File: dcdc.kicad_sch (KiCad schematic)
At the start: 199 parts, among them U11 SIC431AED-T1-GE3, U12 SIC431AED-T1-GE3, U13 SIC431AED-T1-GE3, U22 INA219AIDCNR, U50 INA219AIDCNR, U60 INA219AIDCNR, U65 SIC431AED-T1-GE3, U66 INA219AIDCNR, U69 TPS564247DRLR, U7 TPS564247DRLR, U75 SIC431AED-T1-GE3, U76 INA219AIDCNR, U8 SIC431AED-T1-GE3

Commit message: Update naming on schematic sheets and PCB, update release date
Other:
- title: Jetson AGX Thor Baseboard -> Antmicro Baseboard for Jetson AGX Thor
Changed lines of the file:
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@@
 	(paper "A3")
 	(title_block
-		(title "Jetson AGX Thor Baseboard")
-		(date "2025-11-03")
+		(title "Antmicro Baseboard for Jetson AGX Thor")
+		(date "2026-02-17")
 		(rev "1.1.0")
 		(company "Antmicro Ltd")

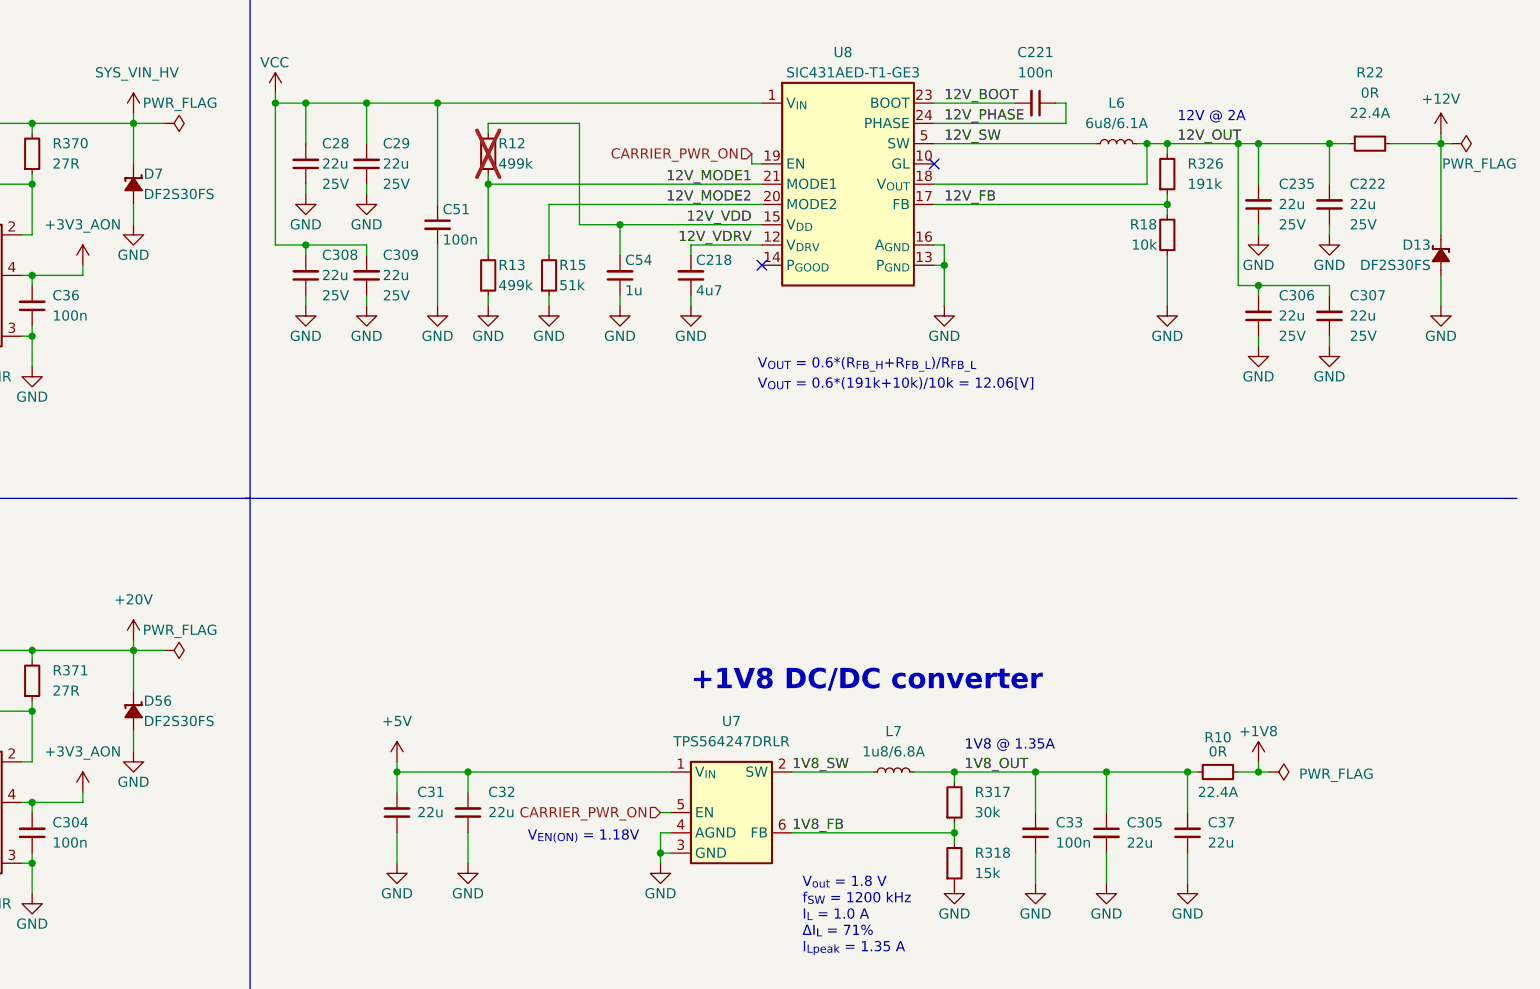
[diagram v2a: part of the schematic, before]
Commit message: [#88664] DF2S30FS diodes replaced by ESDA25P35-1U1M
DF2S30FS -> ESDA25P35-1U1M, changes done on schematics and PCB editor
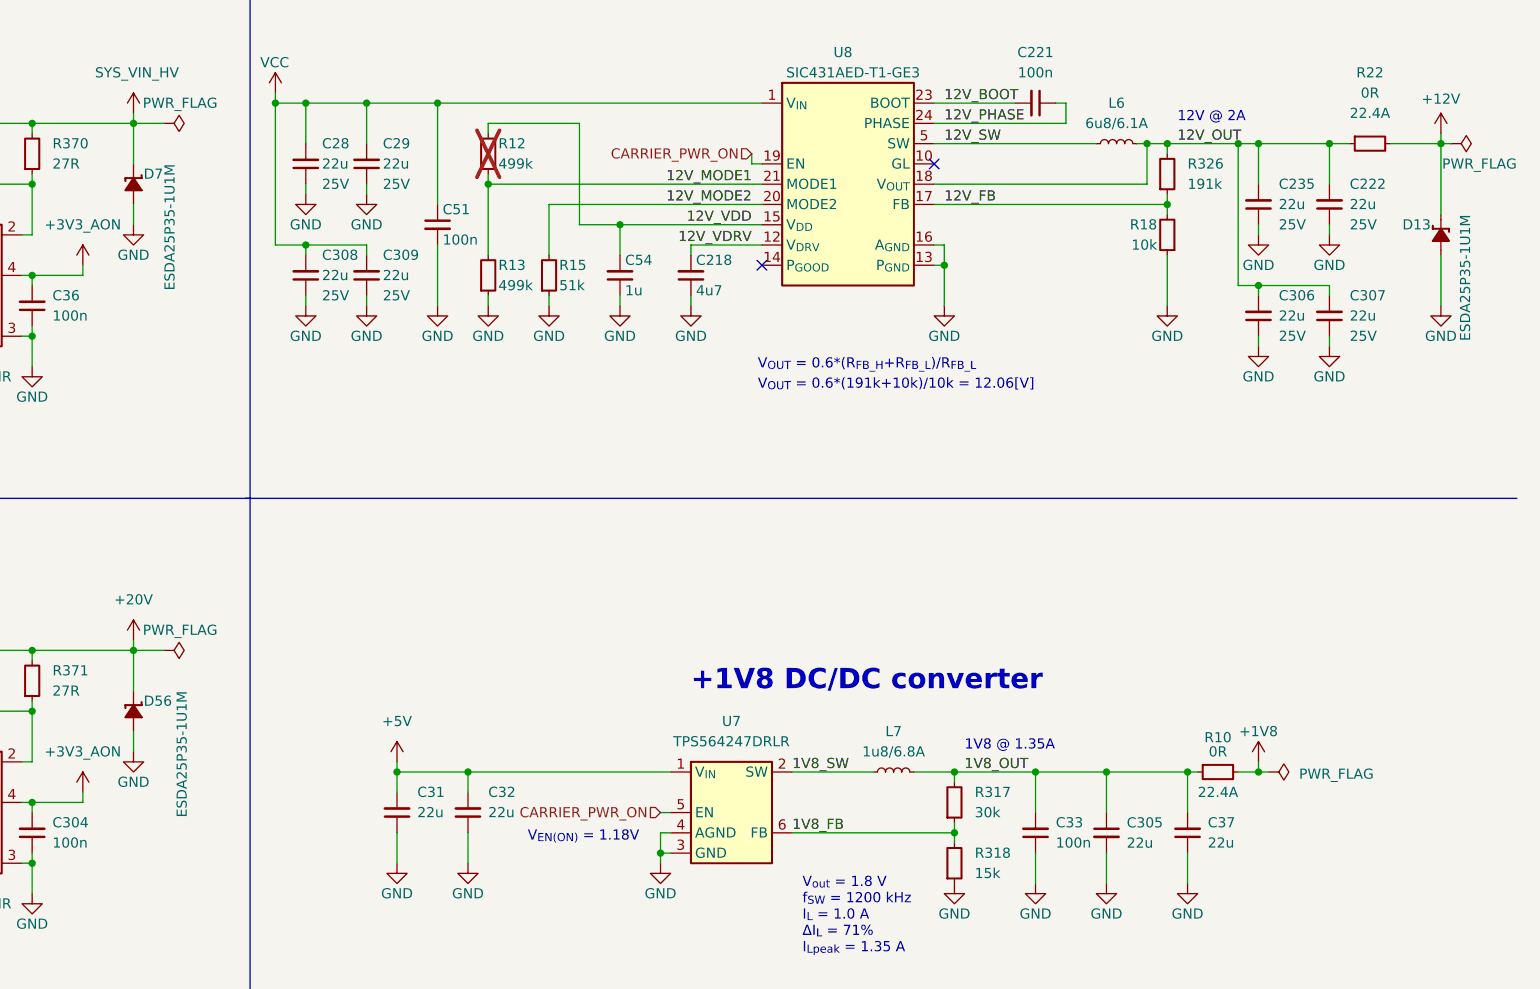
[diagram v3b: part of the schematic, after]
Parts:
- D13, D56, D7: value DF2S30FS_SOD -> ESDA25P35-1U1M; footprint antmicro-footprints:SOD-923 -> antmicro-footprints:QFN-2L_1.6x1x0.55mm; symbol antmicroTVSDiodes:DF2S30FS_SOD -> antmicroTVSDiodes:ESDA25P35-1U1M; MPN DF2S30FS -> ESDA25P35-1U1M; Manufacturer Toshiba -> STMicroelectronics
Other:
- moved on the sheet: D13
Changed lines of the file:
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@@
 	(wire
 		(pts
-			(xy 397.51 38.1) (xy 397.51 49.53)
+			(xy 397.51 38.1) (xy 397.51 46.99)
 		)
 		(stroke
@@
 	(wire
 		(pts
-			(xy 397.51 54.61) (xy 397.51 58.42)
+			(xy 397.51 52.07) (xy 397.51 58.42)
 		)
 		(stroke
@@
 	)
 	(symbol
-		(lib_id "antmicroTVSDiodes:DF2S30FS_SOD")
+		(lib_id "antmicroTVSDiodes:ESDA25P35-1U1M")
 		(at 233.68 40.64 270)
 		(unit 1)
@@
 			)
 		)
-		(property "Value" "DF2S30FS_SOD"
+		(property "Value" "ESDA25P35-1U1M"
 			(at 218.44 62.23 0)
 			(effects
@@
 			)
 		)
-		(property "Footprint" "antmicro-footprints:SOD-923"
-			(at 226.06 62.23 0)
+		(property "Footprint" "antmicro-footprints:QFN-2L_1.6x1x0.55mm"
+			(at 223.52 64.77 0)
 			(effects
 				(font
@@
 			)
 		)
-		(property "Datasheet" "https://toshiba.semicon-storage.com/info/DF2S30FS_datasheet_en_20211216.pdf?did=11156&prodName=DF2S30FS"
-			(at 223.52 62.23 0)
+		(property "Datasheet" "https://www.st.com/resource/en/datasheet/esda25p35-1u1m.pdf"
+			(at 220.98 64.77 0)
 			(effects
 				(font
@@
 			)
 		)
-		(property "Description" "Unidirectional TVS, 8 kV,  SOD-923, 23 V, 7 pF"
-			(at 233.68 40.64 0)
+		(property "Description" "Unidirectional TVS, 30 kV, QFN-2L, 22 V, 195 pF"
+			(at 208.28 64.77 0)
 			(effects
 				(font
 					(size 1.27 1.27)
 				)
+				(justify left bottom)
 				(hide yes)
 			)
 		)
-		(property "Manufacturer" "Toshiba"
-			(at 220.98 62.23 0)
+		(property "Manufacturer" "STMicroelectronics"
+			(at 215.9 64.77 0)
 			(effects
 				(font
@@
 			)
 		)
-		(property "MPN" "DF2S30FS"
-			(at 234.95 44.45 90)
+		(property "MPN" "ESDA25P35-1U1M"
+			(at 237.49 40.64 0)
 			(effects
 				(font
@@
 					(thickness 0.15)
 				)
-				(justify left)
+				(justify left bottom)
 			)
 		)
 		(property "Author" "Antmicro"
-			(at 215.9 62.23 0)
+			(at 213.36 64.77 0)
 			(effects
 				(font
@@
 		)
 		(property "License" "Apache-2.0"
-			(at 213.36 62.23 0)
+			(at 210.82 64.77 0)
 			(effects
 				(font
@@
 	)
 	(symbol
-		(lib_id "antmicroTVSDiodes:DF2S30FS_SOD")
-		(at 397.51 49.53 90)
+		(lib_id "antmicroTVSDiodes:ESDA25P35-1U1M")
+		(at 397.51 46.99 90)
 		(mirror x)
 		(unit 1)
@@
 		(dnp no)
 		(property "Reference" "D13"
-			(at 396.24 50.8 90)
+			(at 396.24 48.26 90)
 			(effects
 				(font
@@
 			)
 		)
-		(property "Value" "DF2S30FS_SOD"
-			(at 412.75 71.12 0)
+		(property "Value" "ESDA25P35-1U1M"
+			(at 412.75 68.58 0)
 			(effects
 				(font
@@
 			)
 		)
-		(property "Footprint" "antmicro-footprints:SOD-923"
-			(at 405.13 71.12 0)
+		(property "Footprint" "antmicro-footprints:QFN-2L_1.6x1x0.55mm"
+			(at 407.67 71.12 0)
 			(effects
 				(font
@@
 			)
 		)
-		(property "Datasheet" "https://toshiba.semicon-storage.com/info/DF2S30FS_datasheet_en_20211216.pdf?did=11156&prodName=DF2S30FS"
-			(at 407.67 71.12 0)
+		(property "Datasheet" "https://www.st.com/resource/en/datasheet/esda25p35-1u1m.pdf"
+			(at 410.21 71.12 0)
 			(effects
 				(font
@@
 			)
 		)
-		(property "Description" "Unidirectional TVS, 8 kV,  SOD-923, 23 V, 7 pF"
-			(at 397.51 49.53 0)
+		(property "Description" "Unidirectional TVS, 30 kV, QFN-2L, 22 V, 195 pF"
+			(at 422.91 71.12 0)
 			(effects
 				(font
 					(size 1.27 1.27)
 				)
+				(justify left bottom)
 				(hide yes)
 			)
 		)
-		(property "Manufacturer" "Toshiba"
-			(at 410.21 71.12 0)
+		(property "Manufacturer" "STMicroelectronics"
+			(at 415.29 71.12 0)
 			(effects
 				(font
@@
 			)
 		)
-		(property "MPN" "DF2S30FS"
-			(at 396.24 53.34 90)
+		(property "MPN" "ESDA25P35-1U1M"
+			(at 401.32 46.99 0)
 			(effects
 				(font
@@
 					(thickness 0.15)
 				)
-				(justify left)
+				(justify left bottom)
 			)
 		)
 		(property "Author" "Antmicro"
-			(at 415.29 71.12 0)
+			(at 417.83 71.12 0)
 			(effects
 				(font
@@
 		)
 		(property "License" "Apache-2.0"
-			(at 417.83 71.12 0)
+			(at 420.37 71.12 0)
 			(effects
 				(font
@@
 	)
 	(symbol
-		(lib_id "antmicroTVSDiodes:DF2S30FS_SOD")
+		(lib_id "antmicroTVSDiodes:ESDA25P35-1U1M")
 		(at 233.68 106.68 270)
 		(unit 1)
@@
 			)
 		)
-		(property "Value" "DF2S30FS_SOD"
+		(property "Value" "ESDA25P35-1U1M"
 			(at 218.44 128.27 0)
 			(effects
@@
 			)
 		)
-		(property "Footprint" "antmicro-footprints:SOD-923"
-			(at 226.06 128.27 0)
+		(property "Footprint" "antmicro-footprints:QFN-2L_1.6x1x0.55mm"
+			(at 223.52 130.81 0)
 			(effects
 				(font
@@
 			)
 		)
-		(property "Datasheet" "https://toshiba.semicon-storage.com/info/DF2S30FS_datasheet_en_20211216.pdf?did=11156&prodName=DF2S30FS"
-			(at 223.52 128.27 0)
+		(property "Datasheet" "https://www.st.com/resource/en/datasheet/esda25p35-1u1m.pdf"
+			(at 220.98 130.81 0)
 			(effects
 				(font
@@
 			)
 		)
-		(property "Description" "Unidirectional TVS, 8 kV,  SOD-923, 23 V, 7 pF"
-			(at 233.68 106.68 0)
+		(property "Description" "Unidirectional TVS, 30 kV, QFN-2L, 22 V, 195 pF"
+			(at 208.28 130.81 0)
 			(effects
 				(font
 					(size 1.27 1.27)
 				)
+				(justify left bottom)
 				(hide yes)
 			)
 		)
-		(property "Manufacturer" "Toshiba"
-			(at 220.98 128.27 0)
+		(property "Manufacturer" "STMicroelectronics"
+			(at 215.9 130.81 0)
 			(effects
 				(font
@@
 			)
 		)
-		(property "MPN" "DF2S30FS"
-			(at 234.95 110.49 90)
+		(property "MPN" "ESDA25P35-1U1M"
+			(at 239.014 106.68 0)
 			(effects
 				(font
@@
 					(thickness 0.15)
 				)
-				(justify left)
+				(justify left bottom)
 			)
 		)
 		(property "Author" "Antmicro"
-			(at 215.9 128.27 0)
+			(at 213.36 130.81 0)
 			(effects
 				(font
@@
 		)
 		(property "License" "Apache-2.0"
-			(at 213.36 128.27 0)
+			(at 210.82 130.81 0)
 			(effects
 				(font

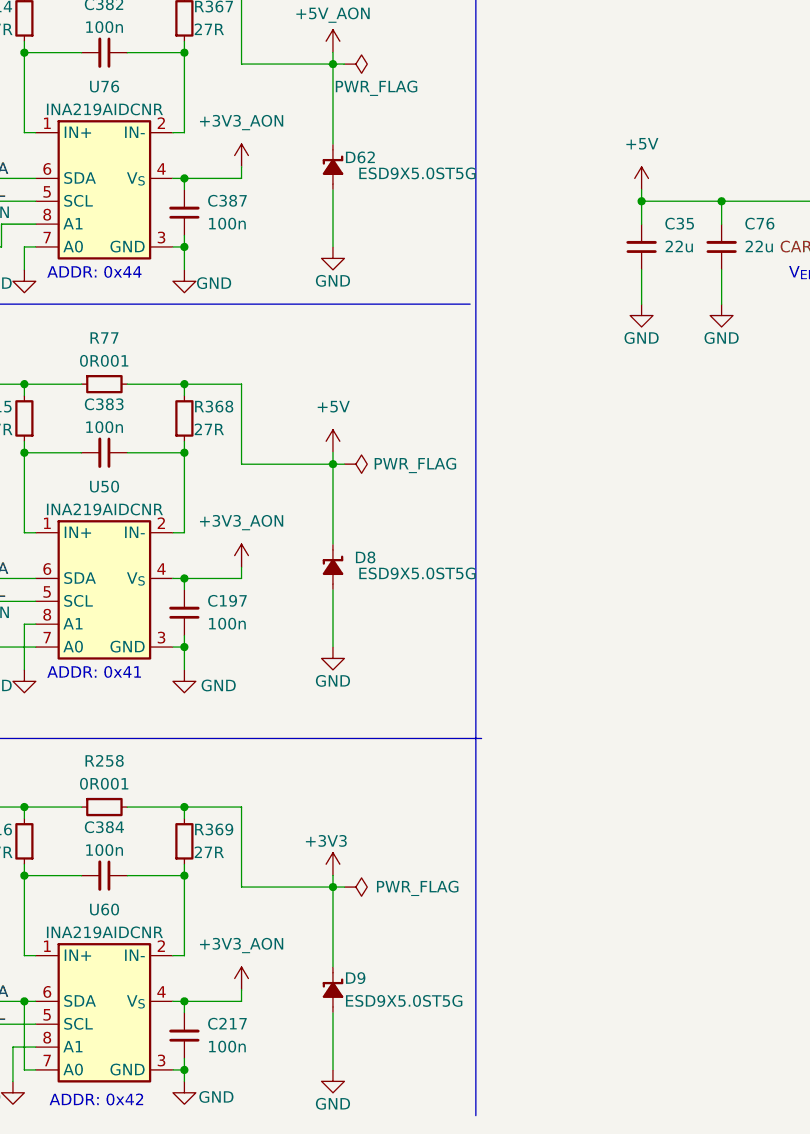
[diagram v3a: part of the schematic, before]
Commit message: [#88664] ESD9X5.0ST5G diodes replaced by PESD5Z5_0F, added TVS on Fan 12V
ESD9X5.0ST5G -> PESD5Z5_0F, changes done on schematics and PCB editor,
added TVS for fan 12V
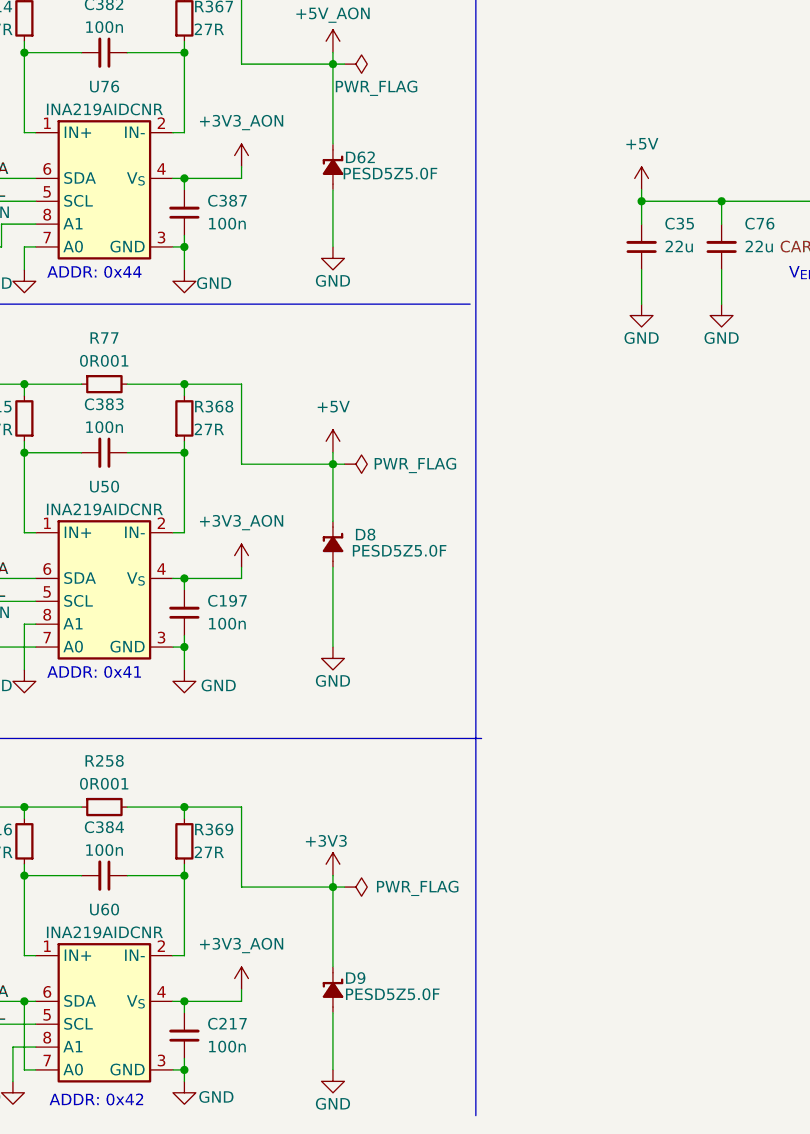
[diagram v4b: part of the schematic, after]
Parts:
- D62, D8, D9: value ESD9X5.0ST5G -> PESD5Z5.0F; footprint antmicro-footprints:SOD-923 -> antmicro-footprints:SOD-523; symbol antmicroTVSDiodes:ESD9X5.0ST5G -> antmicroTVSDiodes:PESD5Z5_0F; MPN ESD9X5.0ST5G -> PESD5Z5.0F; Manufacturer ON Semiconductor -> Nexperia
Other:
- moved on the sheet: D8
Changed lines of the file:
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@@
 	(wire
 		(pts
-			(xy 232.41 226.06) (xy 232.41 232.41)
+			(xy 232.41 223.52) (xy 232.41 232.41)
 		)
 		(stroke
@@
 	(wire
 		(pts
-			(xy 232.41 212.09) (xy 232.41 220.98)
+			(xy 232.41 212.09) (xy 232.41 218.44)
 		)
 		(stroke
@@
 	)
 	(symbol
-		(lib_id "antmicroTVSDiodes:ESD9X5.0ST5G")
-		(at 232.41 220.98 270)
+		(lib_id "antmicroTVSDiodes:PESD5Z5_0F")
+		(at 232.41 218.44 270)
 		(unit 1)
 		(exclude_from_sim no)
@@
 		(dnp no)
 		(property "Reference" "D8"
-			(at 237.236 222.504 90)
+			(at 237.236 219.964 90)
 			(effects
 				(font
@@
 			)
 		)
-		(property "Value" "ESD9X5.0ST5G"
-			(at 217.17 242.57 0)
+		(property "Value" "PESD5Z5.0F"
+			(at 217.17 240.03 0)
 			(effects
 				(font
@@
 			)
 		)
-		(property "Footprint" "antmicro-footprints:SOD-923"
-			(at 224.79 242.57 0)
+		(property "Footprint" "antmicro-footprints:SOD-523"
+			(at 227.33 233.68 0)
 			(effects
 				(font
@@
 			)
 		)
-		(property "Datasheet" "https://www.onsemi.com/pdf/datasheet/esd9x3.3st5g-d.pdf"
-			(at 222.25 242.57 0)
+		(property "Datasheet" "https://assets.nexperia.com/documents/data-sheet/PESD5Z5_0.pdf"
+			(at 224.79 233.68 0)
 			(effects
 				(font
@@
 			)
 		)
-		(property "Description" "Unidirectional TVS, 30 kV,  SOD-923, 5 V, 65 pF"
-			(at 232.41 220.98 0)
+		(property "Description" "Unidirectional TVS, 30 kV,  SOD-523, 5 V, 89 pF"
+			(at 212.09 233.68 0)
 			(effects
 				(font
 					(size 1.27 1.27)
 				)
+				(justify left bottom)
 				(hide yes)
 			)
 		)
-		(property "Manufacturer" "ON Semiconductor"
-			(at 219.71 242.57 0)
+		(property "Manufacturer" "Nexperia"
+			(at 222.25 233.68 0)
 			(effects
 				(font
@@
 			)
 		)
-		(property "MPN" "ESD9X5.0ST5G"
-			(at 248.412 224.282 90)
+		(property "MPN" "PESD5Z5.0F"
+			(at 234.442 222.504 90)
 			(effects
 				(font
@@
 					(thickness 0.15)
 				)
-				(justify right)
+				(justify left bottom)
 			)
 		)
 		(property "Author" "Antmicro"
-			(at 214.63 242.57 0)
+			(at 217.17 233.68 0)
 			(effects
 				(font
@@
 		)
 		(property "License" "Apache-2.0"
-			(at 212.09 242.57 0)
+			(at 214.63 233.68 0)
 			(effects
 				(font
@@
 	)
 	(symbol
-		(lib_id "antmicroTVSDiodes:ESD9X5.0ST5G")
+		(lib_id "antmicroTVSDiodes:PESD5Z5_0F")
 		(at 232.41 176.53 270)
 		(unit 1)
@@
 			)
 		)
-		(property "Value" "ESD9X5.0ST5G"
+		(property "Value" "PESD5Z5.0F"
 			(at 217.17 198.12 0)
 			(effects
@@
 			)
 		)
-		(property "Footprint" "antmicro-footprints:SOD-923"
-			(at 224.79 198.12 0)
+		(property "Footprint" "antmicro-footprints:SOD-523"
+			(at 227.33 191.77 0)
 			(effects
 				(font
@@
 			)
 		)
-		(property "Datasheet" "https://www.onsemi.com/pdf/datasheet/esd9x3.3st5g-d.pdf"
-			(at 222.25 198.12 0)
+		(property "Datasheet" "https://assets.nexperia.com/documents/data-sheet/PESD5Z5_0.pdf"
+			(at 224.79 191.77 0)
 			(effects
 				(font
@@
 			)
 		)
-		(property "Description" "Unidirectional TVS, 30 kV,  SOD-923, 5 V, 65 pF"
-			(at 232.41 176.53 0)
+		(property "Description" "Unidirectional TVS, 30 kV,  SOD-523, 5 V, 89 pF"
+			(at 212.09 191.77 0)
 			(effects
 				(font
 					(size 1.27 1.27)
 				)
+				(justify left bottom)
 				(hide yes)
 			)
 		)
-		(property "Manufacturer" "ON Semiconductor"
-			(at 219.71 198.12 0)
+		(property "Manufacturer" "Nexperia"
+			(at 222.25 191.77 0)
 			(effects
 				(font
@@
 			)
 		)
-		(property "MPN" "ESD9X5.0ST5G"
-			(at 248.412 179.832 90)
+		(property "MPN" "PESD5Z5.0F"
+			(at 233.426 180.594 90)
 			(effects
 				(font
@@
 					(thickness 0.15)
 				)
-				(justify right)
+				(justify left bottom)
 			)
 		)
 		(property "Author" "Antmicro"
-			(at 214.63 198.12 0)
+			(at 217.17 191.77 0)
 			(effects
 				(font
@@
 		)
 		(property "License" "Apache-2.0"
-			(at 212.09 198.12 0)
+			(at 214.63 191.77 0)
 			(effects
 				(font
@@
 	)
 	(symbol
-		(lib_id "antmicroTVSDiodes:ESD9X5.0ST5G")
+		(lib_id "antmicroTVSDiodes:PESD5Z5_0F")
 		(at 232.41 267.97 270)
 		(unit 1)
@@
 			)
 		)
-		(property "Value" "ESD9X5.0ST5G"
+		(property "Value" "PESD5Z5.0F"
 			(at 217.17 289.56 0)
 			(effects
@@
 			)
 		)
-		(property "Footprint" "antmicro-footprints:SOD-923"
-			(at 224.79 289.56 0)
+		(property "Footprint" "antmicro-footprints:SOD-523"
+			(at 227.33 283.21 0)
 			(effects
 				(font
@@
 			)
 		)
-		(property "Datasheet" "https://www.onsemi.com/pdf/datasheet/esd9x3.3st5g-d.pdf"
-			(at 222.25 289.56 0)
+		(property "Datasheet" "https://assets.nexperia.com/documents/data-sheet/PESD5Z5_0.pdf"
+			(at 224.79 283.21 0)
 			(effects
 				(font
@@
 			)
 		)
-		(property "Description" "Unidirectional TVS, 30 kV,  SOD-923, 5 V, 65 pF"
-			(at 232.41 267.97 0)
+		(property "Description" "Unidirectional TVS, 30 kV,  SOD-523, 5 V, 89 pF"
+			(at 212.09 283.21 0)
 			(effects
 				(font
 					(size 1.27 1.27)
 				)
+				(justify left bottom)
 				(hide yes)
 			)
 		)
-		(property "Manufacturer" "ON Semiconductor"
-			(at 219.71 289.56 0)
+		(property "Manufacturer" "Nexperia"
+			(at 222.25 283.21 0)
 			(effects
 				(font
@@
 			)
 		)
-		(property "MPN" "ESD9X5.0ST5G"
+		(property "MPN" "PESD5Z5.0F"
 			(at 233.68 271.78 90)
 			(effects
@@
 					(thickness 0.15)
 				)
-				(justify left)
+				(justify left bottom)
 			)
 		)
 		(property "Author" "Antmicro"
-			(at 214.63 289.56 0)
+			(at 217.17 283.21 0)
 			(effects
 				(font
@@
 		)
 		(property "License" "Apache-2.0"
-			(at 212.09 289.56 0)
+			(at 214.63 283.21 0)
 			(effects
 				(font
